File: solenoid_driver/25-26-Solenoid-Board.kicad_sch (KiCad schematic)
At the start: 17 parts, among them J1 xt30, J2 JST-PH-K, J3 Screw_Terminal_01x08, U1 Teensy4.1, U2 LD1117S50TR_SOT223, U3 PTCAN3414DDFR, U4 ULN2308C

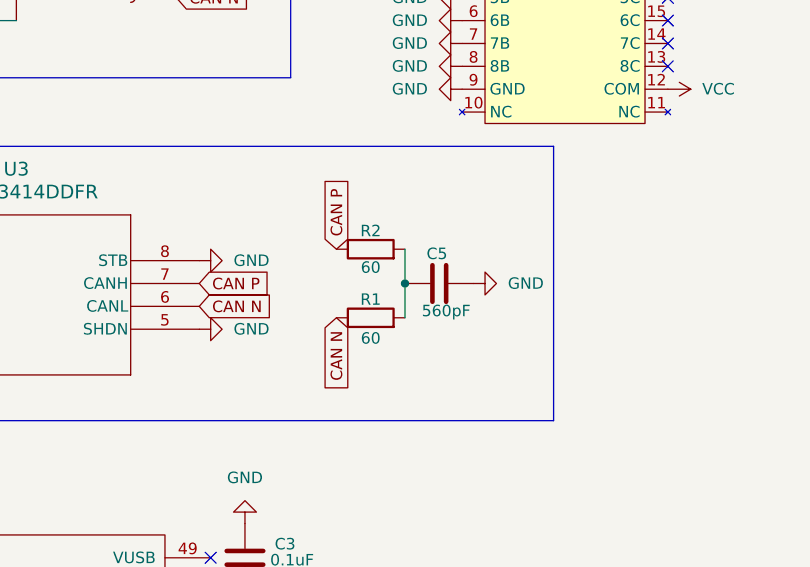
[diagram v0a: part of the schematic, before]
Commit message: Fixed what Sylvestor brought up
fixed tcan package, set 3d models, moved a few things around, and set supplementary circuits as do not populate.

did not add the mentioned diode
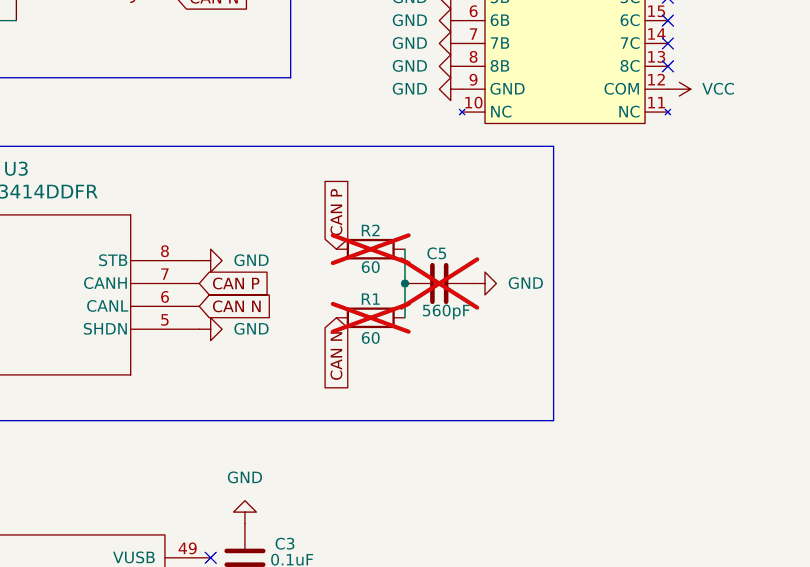
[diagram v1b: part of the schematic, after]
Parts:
- C5, R1, R2: now not fitted
- U3: footprint TCAN:SOT-23-THIN-8_DDF_TEX -> Package_SO:SOIC-8_3.9x4.9mm_P1.27mm
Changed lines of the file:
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@@
 		(in_bom yes)
 		(on_board yes)
-		(dnp no)
+		(dnp yes)
 		(property "Reference" "R1"
 			(at 97.79 70.358 90)
@@
 		(in_bom yes)
 		(on_board yes)
-		(dnp no)
+		(dnp yes)
 		(property "Reference" "R2"
 			(at 97.79 62.738 90)
@@
 			)
 		)
-		(property "Footprint" "TCAN:SOT-23-THIN-8_DDF_TEX"
+		(property "Footprint" "Package_SO:SOIC-8_3.9x4.9mm_P1.27mm"
 			(at 38.1 66.04 0)
 			(effects
@@
 		(in_bom yes)
 		(on_board yes)
-		(dnp no)
+		(dnp yes)
 		(property "Reference" "C5"
 			(at 105.156 65.278 90)
